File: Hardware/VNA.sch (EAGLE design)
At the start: 588 parts, among them IC1 MIC2253, IC10 MAX2871, IC11 RFSW6042, IC12 RFSW6042, IC13 QPC6324, IC14 RFSA3714, IC15 TRF37A73, IC16 QPC6324, IC17 QPC6324, IC18 QPC6324, IC19 AP2114H, IC2 LM3370SD-4221, IC20 NCP702-3.3, IC21 MAX2871, IC22 LT5560, IC23 THS4521IDGKR, IC24 ADL5801, IC25 NCP702-1.8, IC26 MCP33131D-10-E/MS, IC27 LT5560, IC28 THS4521IDGKR, IC29 ADL5801, IC3 LDL212PU50R, IC30 NCP702-1.8, IC31 MCP33131D-10-E/MS, IC32 THS4521IDGKR, IC33 ADL5801, IC34 NCP702-1.8, IC35 MCP33131D-10-E/MS, IC36 LT5560, IC37 STM32G431CB, IC4 LDL212PU50R, IC5 LDL212PU50R, IC6 LDL212PU50R, IC7 SI5351C, IC8 AP2114H, IC9 NCP702-3.3, J1 PJ-014D, J2 AMPHENOL_132289, J3 AMPHENOL_132289, J4 TYPE-C16P(073), Q1 SSM3J338R, Q2 SSM3J338R, T1 B012-617DB-1-63-B331, T2 B012-617DB-1-63-B331, T3 B012-617DB-1-63-B331, U1 W25Q16BVSN, U2 6SLX9TQG144, X1 SMA_CONNECTOR, X2 SMA_CONNECTOR, Y1 DSB221SDN/26MHz

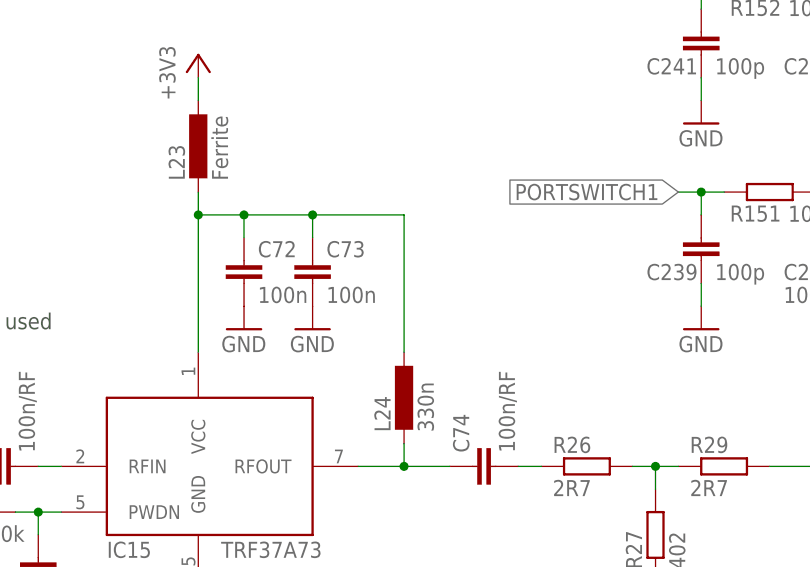
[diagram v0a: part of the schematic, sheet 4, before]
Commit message: Bugfixes DC jack/amplifier
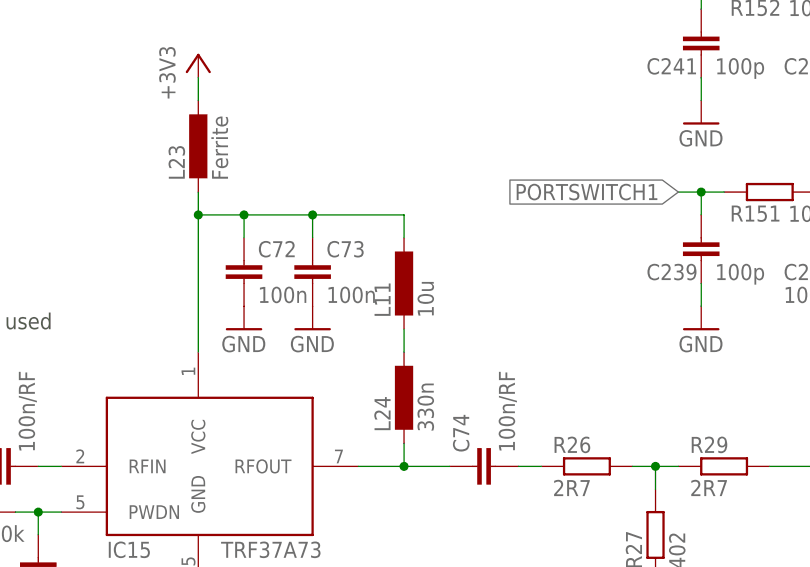
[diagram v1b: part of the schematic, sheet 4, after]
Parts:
- added L11: 10u, VNA:INDUCTOR
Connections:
- new net N$270: L11.2, L24.1
- net GND: now also J1.2; no longer J1.3
- net N$152: now also L11.1; no longer L24.1
- net N$168: now also J1.3; no longer J1.2

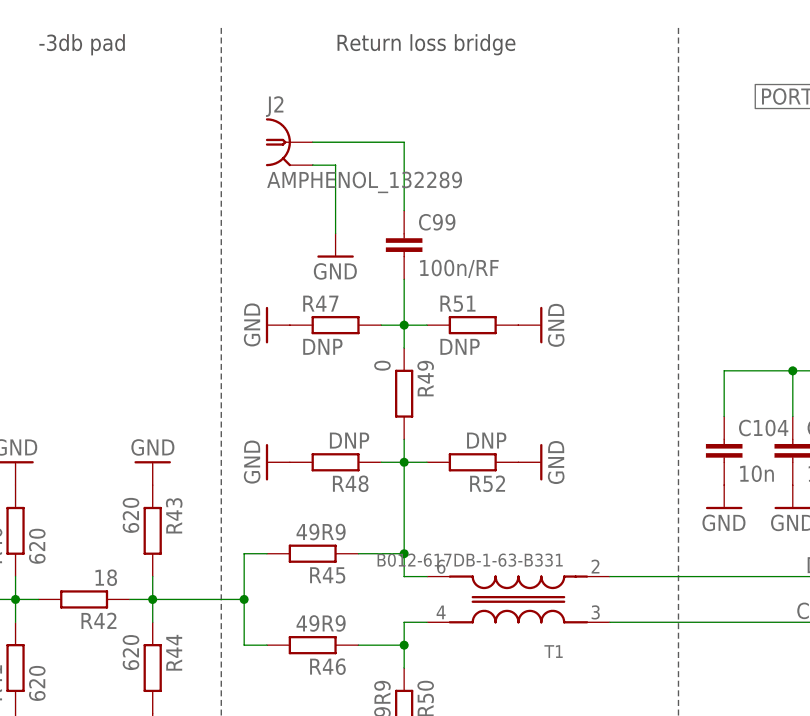
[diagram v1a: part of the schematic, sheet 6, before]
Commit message: Ripup connections and prepare for 6 layer layout
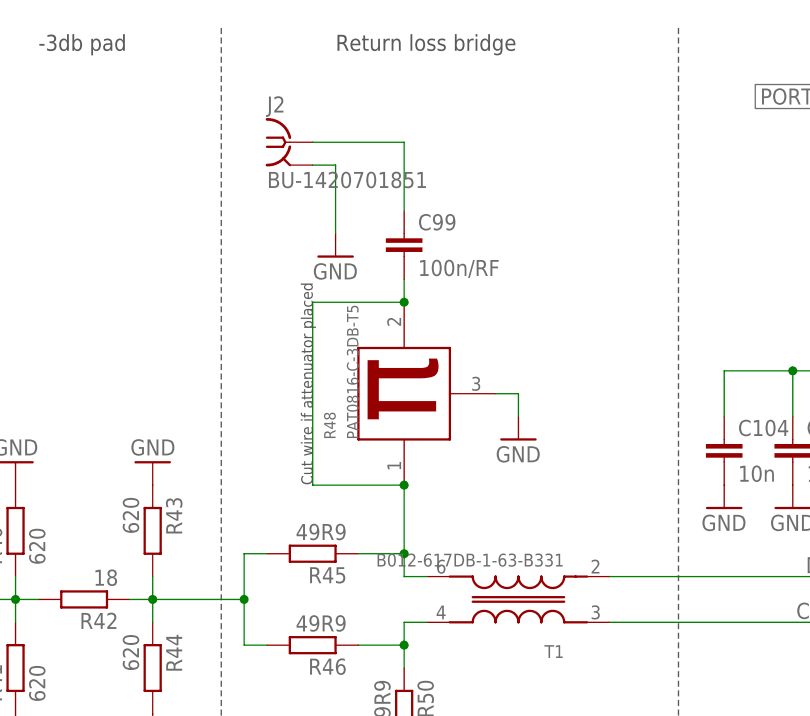
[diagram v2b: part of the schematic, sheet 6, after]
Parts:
- removed R49, R77: 0, VNA:R-EU_R0402
- removed R51, R52, R74, R75, R78, R79: DNP, VNA:R-EU_R0402
- J2, J3: value AMPHENOL_132289 -> BU-1420701851; device VNA:AMPHENOL_132289 -> VNA:BU-1420701851
- R47, R48: value DNP -> PAT0816-C-3DB-T5; device VNA:R-EU_R0402 -> VNA:PAT0816-C-3DB-T5
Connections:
- removed net N$236: C99.2, R47.2, R49.1, R51.1
- removed net N$238: C136.2, R74.2, R77.1, R78.1
- removed net N$25: R72.1, R75.1, R77.2, R79.2, T2.OUT+
- new net N$271: C99.2, R45.1, R48.IN, R48.OUT, T1.OUT-
- net GND: now also R47.GND, R48.GND; no longer R47.1, R48.2, R51.2, R52.1, R74.1, R75.2, R78.2, R79.1
- net N$4: now also C136.2, R47.IN, R47.OUT, R72.1, T2.OUT+; no longer R45.1, R48.1, R49.2, R52.2, T1.OUT-
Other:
- note added: "Cut wire if attenuator placed"

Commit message: Routing
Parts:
- added L12, L13, L15, L16, L17, L54, L55, L56, L57, L58, L59, L60, L61, L62, L63: Ferrite, VNA:FERRITE
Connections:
- new net N$236: C129.1, IC25.EN, IC25.VIN, IC26.VREF, L13.1
- new net N$238: C119.1, C122.1, L16.1, L32.1, L33.1
- new net N$25: C102.2, C103.2, IC22.VCC, L12.1, R53.1, R54.1
- new net N$272: C115.2, IC23.V+, L15.1
- new net N$273: C104.1, C105.1, C106.1, C108.1, C111.1, IC24.VPDT, IC24.VPLO, IC24.VPRF, L17.1
- new net N$274: C141.1, C142.1, C143.1, C145.1, C148.1, IC29.VPDT, IC29.VPLO, IC29.VPRF, L54.1
- new net N$275: C156.1, C159.1, L40.1, L41.1, L55.1
- new net N$276: C152.2, IC28.V+, L56.1
- new net N$277: C139.2, C140.2, IC27.VCC, L57.1, R80.1, R81.1
- new net N$278: C166.1, IC30.EN, IC30.VIN, IC31.VREF, L58.1
- new net N$279: C171.1, C172.1, C175.1, C177.1, C180.1, IC33.VPDT, IC33.VPLO, IC33.VPRF, L59.1
- new net N$280: C190.1, C193.1, L46.1, L47.1, L60.1
- new net N$281: C204.2, C205.2, IC36.VCC, L61.1, R102.1, R103.1
- new net N$282: C181.2, IC32.V+, L62.1
- new net N$283: C195.1, IC34.EN, IC34.VIN, IC35.VREF, L63.2
- net +5V/1: now also L12.2, L13.2, L15.2, L16.2, L17.2; no longer C102.2, C103.2, C104.1, C105.1, C106.1, C108.1, C111.1, C115.2, C119.1, C122.1, C129.1, IC22.VCC, IC23.V+, IC24.VPDT, IC24.VPLO, IC24.VPRF, IC25.EN, IC25.VIN, IC26.VREF, L32.1, L33.1, R53.1, R54.1
- net +5V/2: now also L54.2, L55.2, L56.2, L57.2, L58.2; no longer C139.2, C140.2, C141.1, C142.1, C143.1, C145.1, C148.1, C152.2, C156.1, C159.1, C166.1, IC27.VCC, IC28.V+, IC29.VPDT, IC29.VPLO, IC29.VPRF, IC30.EN, IC30.VIN, IC31.VREF, L40.1, L41.1, R80.1, R81.1
- net +5V/3: now also L59.2, L60.2, L61.2, L62.2, L63.1; no longer C171.1, C172.1, C175.1, C177.1, C180.1, C181.2, C190.1, C193.1, C195.1, C204.2, C205.2, IC32.V+, IC33.VPDT, IC33.VPLO, IC33.VPRF, IC34.EN, IC34.VIN, IC35.VREF, IC36.VCC, L46.1, L47.1, R102.1, R103.1
- net PORT1LO1: now also IC21.RFOUTA_P, R32.1; no longer IC21.RFOUTA_N, R33.1
- net REFLO1: now also IC21.RFOUTA_N, R33.1; no longer IC21.RFOUTA_P, R32.1
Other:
- moved on the sheet: C115, C152, C181

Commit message: layout work
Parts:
- removed R41, R43, R44, R67, R68, R70, R71: 620, VNA:R-EU_R0402
- removed R42, R69: 18, VNA:R-EU_R0402
- added R49: PAT0816-C-3DB-T5, VNA:PAT0816-C-3DB-T5
- R40: value 620 -> PAT0816-C-3DB-T5; device VNA:R-EU_R0402 -> VNA:PAT0816-C-3DB-T5
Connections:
- net GND: now also R40.GND, R49.GND; no longer R40.2, R41.1, R43.1, R44.2, R67.2, R68.1, R70.1, R71.2
- net N$1: now also R49.IN; no longer R40.1, R41.2, R42.2
- net N$2: now also R49.OUT; no longer R42.1, R43.2, R44.1
- net N$21: now also R40.OUT; no longer R67.1, R68.2, R69.2
- net N$22: now also R40.IN; no longer R69.1, R70.2, R71.1

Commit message: layout work
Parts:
- added L64, L65: Ferrite, VNA:FERRITE
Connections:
- new net N$320: C54.1, C55.1, IC10.VCC_DIG, IC10.VDD_SD, L64.1
- new net N$322: C83.1, C84.1, IC21.VCC_DIG, IC21.VDD_SD, L65.1
- net +3V3: now also L64.2, L65.2; no longer C54.1, C55.1, C83.1, C84.1, IC10.VCC_DIG, IC10.VDD_SD, IC21.VCC_DIG, IC21.VDD_SD
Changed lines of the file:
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@@
 <part name="R40" library="VNA" library_urn="urn:adsk.eagle:library:22367181" deviceset="PAT0816-C-3DB-T5" device=""/>
 <part name="GND135" library="VNA" library_urn="urn:adsk.eagle:library:22367181" deviceset="GND" device=""/>
+<part name="L64" library="VNA" library_urn="urn:adsk.eagle:library:22367181" deviceset="FERRITE" device="" package3d_urn="urn:adsk.eagle:package:22367274/3" value="Ferrite"/>
+<part name="L65" library="VNA" library_urn="urn:adsk.eagle:library:22367181" deviceset="FERRITE" device="" package3d_urn="urn:adsk.eagle:package:22367274/3" value="Ferrite"/>
 </parts>
 <sheets>
@@
 <attribute name="VALUE" x="71.12" y="213.995" size="1.778" layer="96"/>
 </instance>
-<instance part="+3V34" gate="G$1" x="111.76" y="167.64" smashed="yes">
-<attribute name="VALUE" x="109.22" y="162.56" size="1.778" layer="96" rot="R90"/>
+<instance part="+3V34" gate="G$1" x="111.76" y="180.34" smashed="yes">
+<attribute name="VALUE" x="109.22" y="175.26" size="1.778" layer="96" rot="R90"/>
 </instance>
 <instance part="L19" gate="G$1" x="106.68" y="210.82" smashed="yes" rot="R90">
@@
 <attribute name="VALUE" x="61.976" y="130.556" size="1.778" layer="96" rot="R180"/>
 </instance>
+<instance part="L64" gate="G$1" x="111.76" y="170.18" smashed="yes" rot="R180">
+<attribute name="NAME" x="113.2586" y="173.99" size="1.778" layer="95" rot="R270"/>
+<attribute name="VALUE" x="108.458" y="173.99" size="1.778" layer="96" rot="R270"/>
+</instance>
 </instances>
 <busses>
@@
 <net name="+3V3" class="0">
 <segment>
-<wire x1="99.06" y1="162.56" x2="104.14" y2="162.56" width="0.1524" layer="91"/>
-<wire x1="104.14" y1="162.56" x2="106.68" y2="162.56" width="0.1524" layer="91"/>
-<wire x1="106.68" y1="162.56" x2="111.76" y2="162.56" width="0.1524" layer="91"/>
-<pinref part="IC10" gate="G$1" pin="VCC_DIG"/>
-<wire x1="106.68" y1="147.32" x2="106.68" y2="162.56" width="0.1524" layer="91"/>
-<junction x="106.68" y="162.56"/>
-<pinref part="IC10" gate="G$1" pin="VDD_SD"/>
-<wire x1="111.76" y1="147.32" x2="111.76" y2="162.56" width="0.1524" layer="91"/>
-<pinref part="C55" gate="G$1" pin="1"/>
-<wire x1="104.14" y1="160.02" x2="104.14" y2="162.56" width="0.1524" layer="91"/>
-<junction x="104.14" y="162.56"/>
-<pinref part="C54" gate="G$1" pin="1"/>
-<wire x1="99.06" y1="160.02" x2="99.06" y2="162.56" width="0.1524" layer="91"/>
 <pinref part="+3V34" gate="G$1" pin="+3V3"/>
-<wire x1="111.76" y1="165.1" x2="111.76" y2="162.56" width="0.1524" layer="91"/>
-<junction x="111.76" y="162.56"/>
+<wire x1="111.76" y1="177.8" x2="111.76" y2="175.26" width="0.1524" layer="91"/>
+<pinref part="L64" gate="G$1" pin="2"/>
 </segment>
 </net>
@@
 </segment>
 </net>
+<net name="N$320" class="0">
+<segment>
+<wire x1="99.06" y1="162.56" x2="104.14" y2="162.56" width="0.1524" layer="91"/>
+<wire x1="104.14" y1="162.56" x2="106.68" y2="162.56" width="0.1524" layer="91"/>
+<wire x1="106.68" y1="162.56" x2="111.76" y2="162.56" width="0.1524" layer="91"/>
+<pinref part="IC10" gate="G$1" pin="VCC_DIG"/>
+<wire x1="106.68" y1="147.32" x2="106.68" y2="162.56" width="0.1524" layer="91"/>
+<junction x="106.68" y="162.56"/>
+<pinref part="IC10" gate="G$1" pin="VDD_SD"/>
+<wire x1="111.76" y1="147.32" x2="111.76" y2="162.56" width="0.1524" layer="91"/>
+<pinref part="C55" gate="G$1" pin="1"/>
+<wire x1="104.14" y1="160.02" x2="104.14" y2="162.56" width="0.1524" layer="91"/>
+<junction x="104.14" y="162.56"/>
+<pinref part="C54" gate="G$1" pin="1"/>
+<wire x1="99.06" y1="160.02" x2="99.06" y2="162.56" width="0.1524" layer="91"/>
+<junction x="111.76" y="162.56"/>
+<wire x1="111.76" y1="165.1" x2="111.76" y2="162.56" width="0.1524" layer="91"/>
+<pinref part="L64" gate="G$1" pin="1"/>
+</segment>
+</net>
 </nets>
 </sheet>
@@
 <attribute name="VALUE" x="99.06" y="213.995" size="1.778" layer="96"/>
 </instance>
-<instance part="+3V311" gate="G$1" x="139.7" y="167.64" smashed="yes">
-<attribute name="VALUE" x="137.16" y="162.56" size="1.778" layer="96" rot="R90"/>
+<instance part="+3V311" gate="G$1" x="139.7" y="180.34" smashed="yes">
+<attribute name="VALUE" x="137.16" y="175.26" size="1.778" layer="96" rot="R90"/>
 </instance>
 <instance part="L28" gate="G$1" x="134.62" y="210.82" smashed="yes" rot="R90">
@@
 <attribute name="VALUE" x="226.06" y="134.62" size="1.778" layer="96"/>
 </instance>
+<instance part="L65" gate="G$1" x="139.7" y="170.18" smashed="yes" rot="R180">
+<attribute name="NAME" x="141.1986" y="173.99" size="1.778" layer="95" rot="R270"/>
+<attribute name="VALUE" x="136.398" y="173.99" size="1.778" layer="96" rot="R270"/>
+</instance>
 </instances>
 <busses>
@@
 <net name="+3V3" class="0">
 <segment>
-<wire x1="127" y1="162.56" x2="132.08" y2="162.56" width="0.1524" layer="91"/>
-<wire x1="132.08" y1="162.56" x2="134.62" y2="162.56" width="0.1524" layer="91"/>
-<wire x1="134.62" y1="162.56" x2="139.7" y2="162.56" width="0.1524" layer="91"/>
-<pinref part="IC21" gate="G$1" pin="VCC_DIG"/>
-<wire x1="134.62" y1="147.32" x2="134.62" y2="162.56" width="0.1524" layer="91"/>
-<junction x="134.62" y="162.56"/>
-<pinref part="IC21" gate="G$1" pin="VDD_SD"/>
-<wire x1="139.7" y1="147.32" x2="139.7" y2="162.56" width="0.1524" layer="91"/>
-<pinref part="C84" gate="G$1" pin="1"/>
-<wire x1="132.08" y1="160.02" x2="132.08" y2="162.56" width="0.1524" layer="91"/>
-<junction x="132.08" y="162.56"/>
-<pinref part="C83" gate="G$1" pin="1"/>
-<wire x1="127" y1="160.02" x2="127" y2="162.56" width="0.1524" layer="91"/>
 <pinref part="+3V311" gate="G$1" pin="+3V3"/>
-<wire x1="139.7" y1="165.1" x2="139.7" y2="162.56" width="0.1524" layer="91"/>
-<junction x="139.7" y="162.56"/>
+<wire x1="139.7" y1="177.8" x2="139.7" y2="175.26" width="0.1524" layer="91"/>
+<pinref part="L65" gate="G$1" pin="2"/>
 </segment>
 </net>
@@
 </segment>
 </net>
+<net name="N$322" class="0">
+<segment>
+<wire x1="127" y1="162.56" x2="132.08" y2="162.56" width="0.1524" layer="91"/>
+<wire x1="132.08" y1="162.56" x2="134.62" y2="162.56" width="0.1524" layer="91"/>
+<wire x1="134.62" y1="162.56" x2="139.7" y2="162.56" width="0.1524" layer="91"/>
+<pinref part="IC21" gate="G$1" pin="VCC_DIG"/>
+<wire x1="134.62" y1="147.32" x2="134.62" y2="162.56" width="0.1524" layer="91"/>
+<junction x="134.62" y="162.56"/>
+<pinref part="IC21" gate="G$1" pin="VDD_SD"/>
+<wire x1="139.7" y1="147.32" x2="139.7" y2="162.56" width="0.1524" layer="91"/>
+<pinref part="C84" gate="G$1" pin="1"/>
+<wire x1="132.08" y1="160.02" x2="132.08" y2="162.56" width="0.1524" layer="91"/>
+<junction x="132.08" y="162.56"/>
+<pinref part="C83" gate="G$1" pin="1"/>
+<wire x1="127" y1="160.02" x2="127" y2="162.56" width="0.1524" layer="91"/>
+<junction x="139.7" y="162.56"/>
+<wire x1="139.7" y1="165.1" x2="139.7" y2="162.56" width="0.1524" layer="91"/>
+<pinref part="L65" gate="G$1" pin="1"/>
+</segment>
+</net>

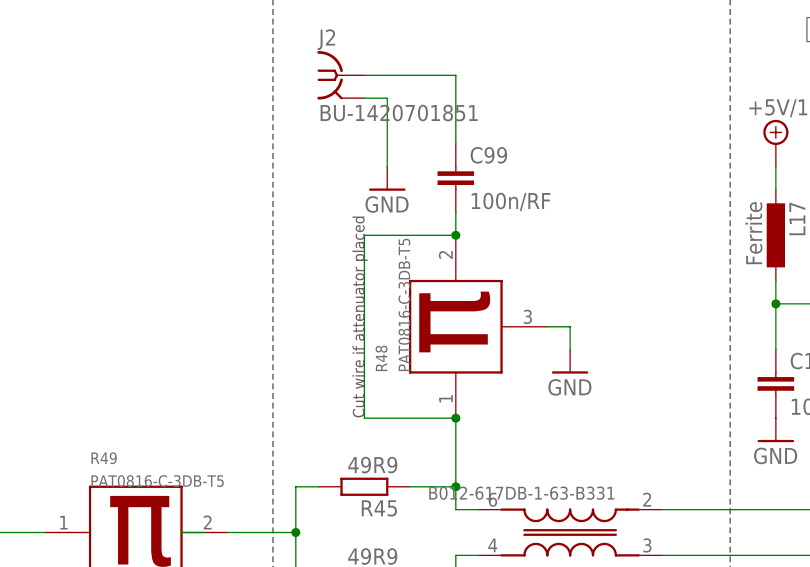
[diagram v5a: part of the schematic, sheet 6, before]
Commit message: 6 layer routing completed
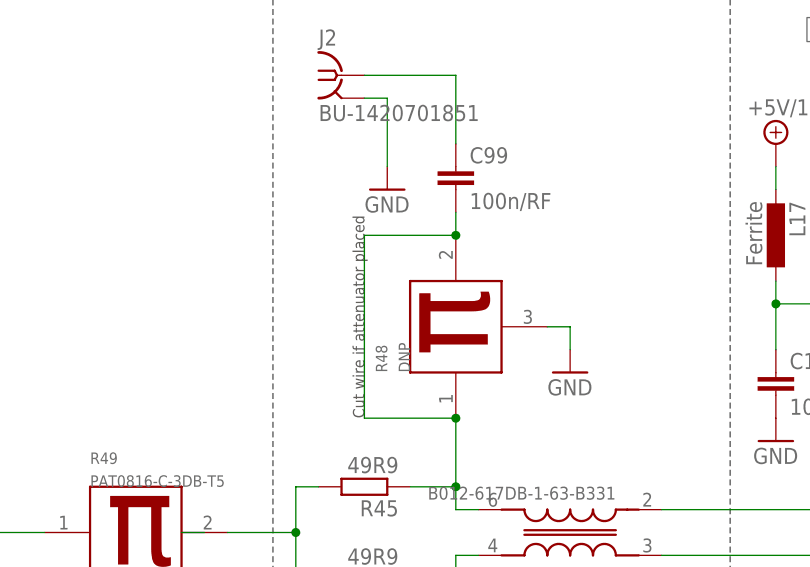
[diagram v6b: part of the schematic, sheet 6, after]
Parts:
- R47, R48: value PAT0816-C-3DB-T5 -> DNP
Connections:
- net N$163 renamed +6V
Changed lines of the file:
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@@
 <part name="GND141" library="VNA" library_urn="urn:adsk.eagle:library:22367181" deviceset="GND" device=""/>
 <part name="GND142" library="VNA" library_urn="urn:adsk.eagle:library:22367181" deviceset="GND" device=""/>
-<part name="R48" library="VNA" library_urn="urn:adsk.eagle:library:22367181" deviceset="PAT0816-C-3DB-T5" device=""/>
-<part name="R47" library="VNA" library_urn="urn:adsk.eagle:library:22367181" deviceset="PAT0816-C-3DB-T5" device=""/>
+<part name="R48" library="VNA" library_urn="urn:adsk.eagle:library:22367181" deviceset="PAT0816-C-3DB-T5" device="" value="DNP"/>
+<part name="R47" library="VNA" library_urn="urn:adsk.eagle:library:22367181" deviceset="PAT0816-C-3DB-T5" device="" value="DNP"/>
 <part name="L12" library="VNA" library_urn="urn:adsk.eagle:library:22367181" deviceset="FERRITE" device="" package3d_urn="urn:adsk.eagle:package:22367274/3" value="Ferrite"/>
 <part name="L13" library="VNA" library_urn="urn:adsk.eagle:library:22367181" deviceset="FERRITE" device="" package3d_urn="urn:adsk.eagle:package:22367274/3" value="Ferrite"/>
@@
 </segment>
 </net>
-<net name="N$163" class="0">
+<net name="+6V" class="0">
 <segment>
 <pinref part="IC4" gate="G$1" pin="VIN"/>
@@
 <wire x1="210.82" y1="170.18" x2="210.82" y2="175.26" width="0.1524" layer="91"/>
 <junction x="210.82" y="175.26"/>
+<label x="236.22" y="175.26" size="1.778" layer="95"/>
 </segment>
 </net>
